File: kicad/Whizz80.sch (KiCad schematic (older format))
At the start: 20 parts, among them J1 Conn_01x24, SW3 SW_Push, U1 74HC139, U2 Z80CPU, U3 CY62256N, U4 28C256

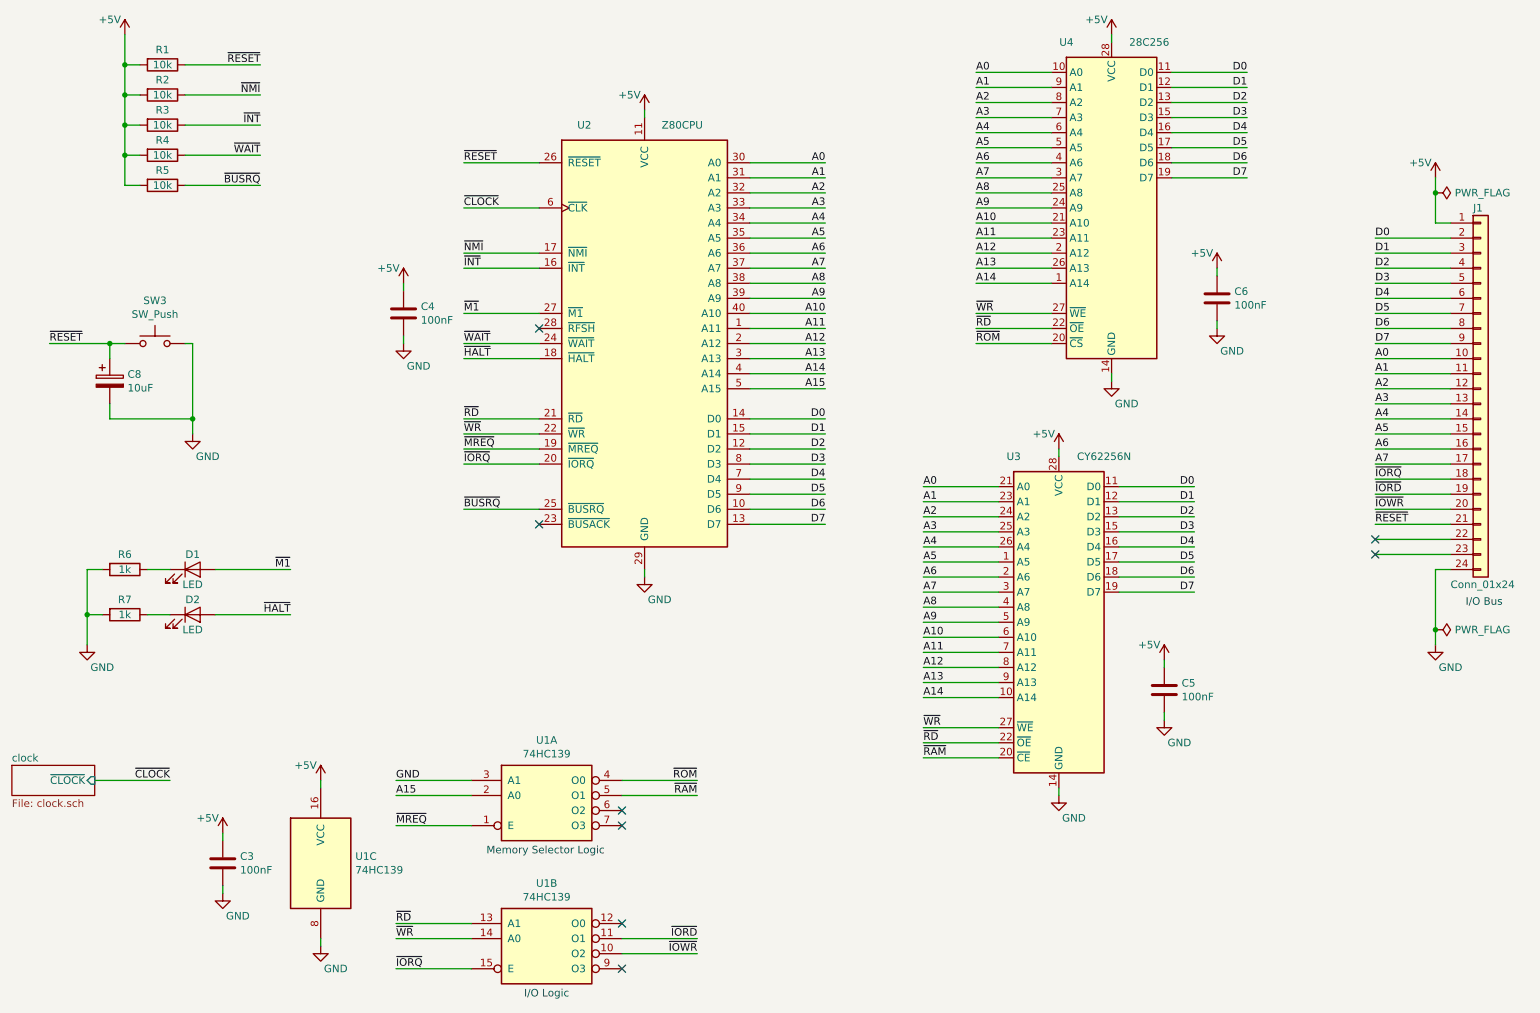
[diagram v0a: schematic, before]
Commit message: Added in extra LEDs to monitor signals with optional jumpers
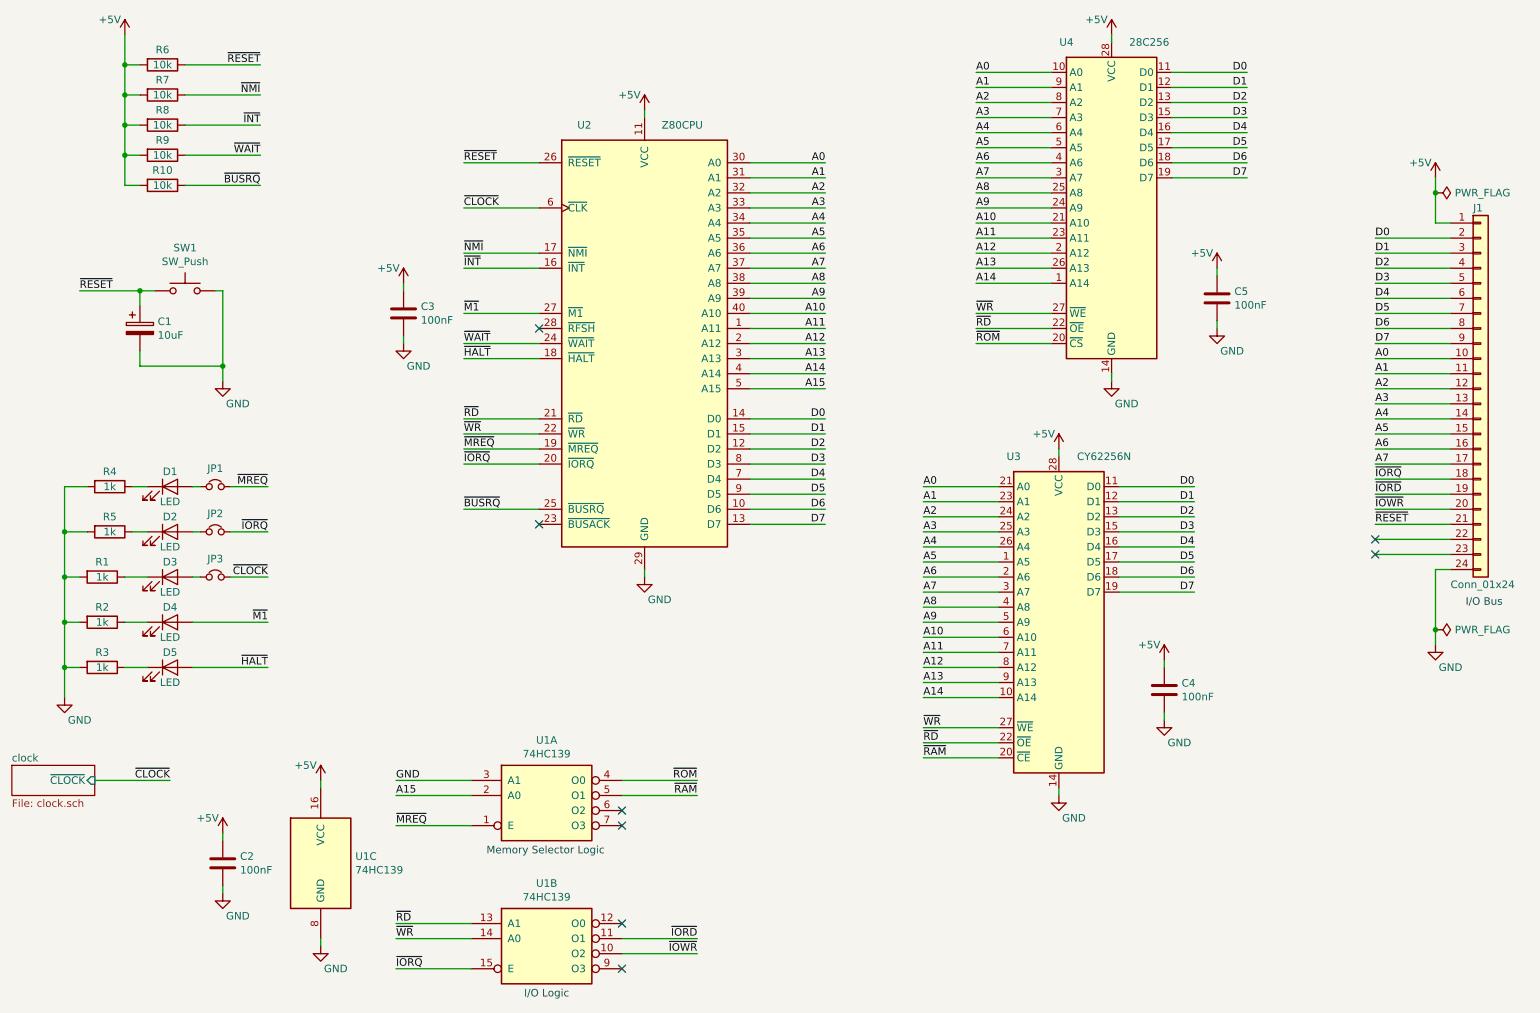
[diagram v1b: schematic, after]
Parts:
- added D1, D2, D3: LED, symbol Device:LED
- added JP1, JP2, JP3: Jumper_NC_Small, symbol Device:Jumper_NC_Small
- added R1, R4, R5: 1k, symbol Whizz80:R
- renumbered C8 to C1, C3 to C2, C4 to C3, C5 to C4, C6 to C5, D1 to D4, D2 to D5, R5 to R10, R6 to R2, R7 to R3, R1 to R6, R2 to R7, R3 to R8, R4 to R9, SW3 to SW1
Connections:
- net GND: now also R1.2, R4.2, R5.2
- net ~CLOCK: now also JP3.2
- net ~IORQ: now also JP2.2
- net ~MREQ: now also JP1.2
- new net: D3.1 (K), R1.1
- new net: D3.2 (A), JP3.1
- new net: D2.1 (K), R5.1
- new net: D2.2 (A), JP2.1
- new net: D1.1 (K), R4.1
- new net: D1.2 (A), JP1.1
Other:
- moved on the sheet: C1, D4, D5, R2, R3, SW1
